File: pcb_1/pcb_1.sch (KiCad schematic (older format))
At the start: 32 parts, among them J1 Vin, J2 Vout, J3 2N3055_conn, P1 CONN_01X07, Q2 BD139, U1 MAX9944ASA+T, U2 MCP3422A0-E/SN, U3 MCP4822-E/SN, U4 INA213AIDCKT, U5 LM7705MM/NOPB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

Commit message: Mittauspinnit lisätty
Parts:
- added Cb6, Cb7: 0.1u, symbol C
- added P2, P3, P4, P5, P6, P7: CONN_01X01, symbol CONN_01X01
- added R6, R7: 10k, symbol R
- added U9: INA240A1PWR, symbol INA240A1PWR
- Rs1: value 0.05 -> 0.1
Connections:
- net +5V: now also U9.5 (OUT), U9.6 (VS)
- net -0.232V: now also P4.1 (P1)
- net GND: now also Cb6.2, Cb7.2, R7.2, U9.4 (NC), U9.7 (REF1)
- net at R3.2, R4.1, U1.2 (INA-)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: now also Cb6.1
- net at Cb2.1, U1.5 (INB+), U2.7 (CH2+): now also R6.2, R7.1; no longer U4.6 (OUT)
- net at Cb4.1, U1.6 (INB-), U3.6 (VoutB): now also P2.1 (P1)
- net at Cb3.1, U1.3 (INA+), U3.8 (VoutA): now also P3.1 (P1)
- net at J3.1, Rs1.1, U4.4 (IN+): now also U9.2 (GND)
- net at J2.2, R3.1, Rs1.2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: now also U9.3 (REF2)
- net at D1.2 (A), R1.1, R2.2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: now also P7.1 (P1)
- new net: R6.1, U4.6 (OUT), U9.8 (IN+)
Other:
- moved on the sheet: J2, R3, R4, U4

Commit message: AC-input lisätty Footprintit mikropiireille
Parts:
- Cb6, Cb7: footprint (none) -> Capacitors_SMD:C_0805_HandSoldering
- P2, P3, P4, P5, P6, P7: footprint (none) -> Pin_Headers:Pin_Header_Straight_1x01_Pitch2.54mm
- R6, R7: footprint (none) -> Resistors_SMD:R_0603_HandSoldering

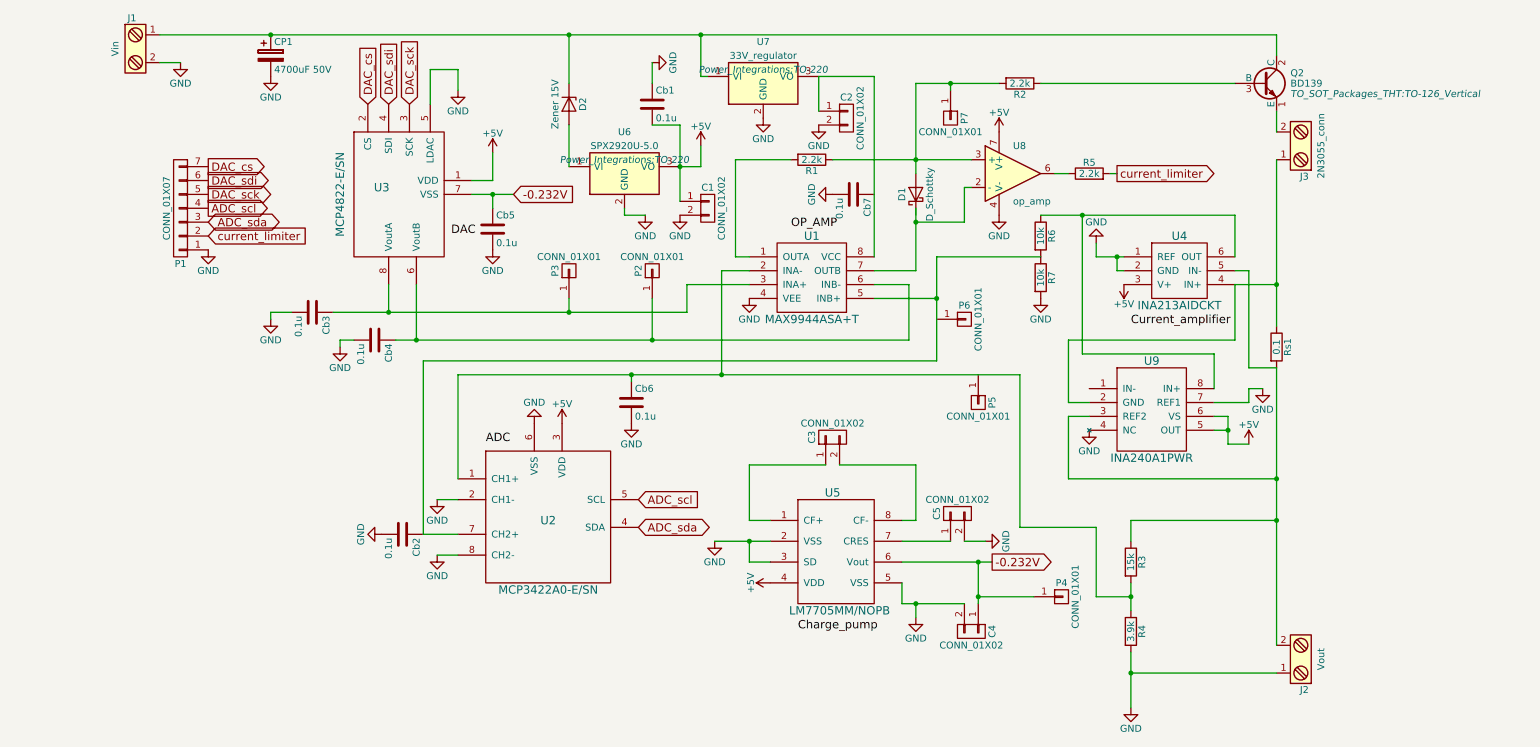
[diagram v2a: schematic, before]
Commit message: -Tasasuuntaajalle footprint footprints kansiossa -Oparille lisätty kapasitpanssipaikkoja
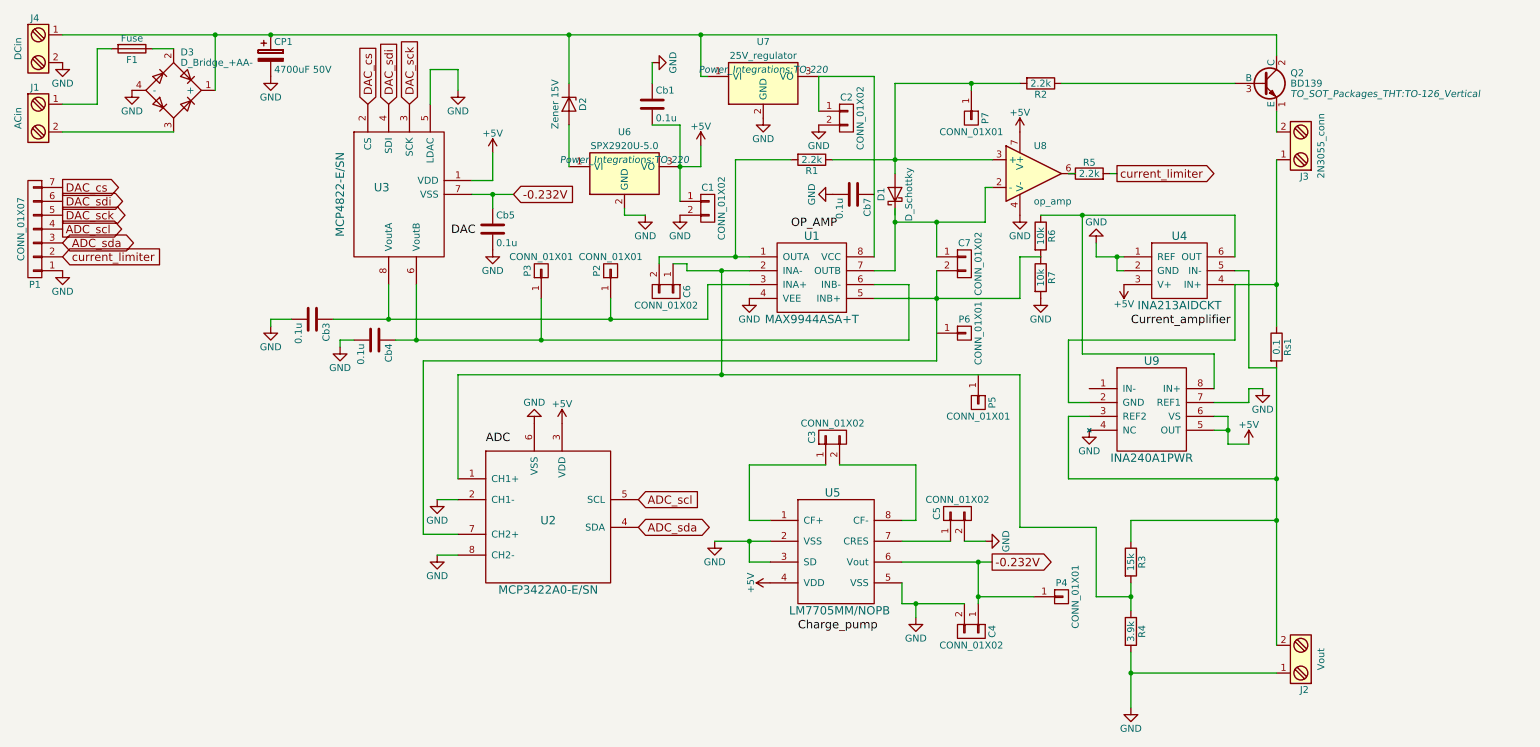
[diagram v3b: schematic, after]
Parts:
- removed Cb2, Cb6: 0.1u, Capacitors_SMD:C_0805_HandSoldering, symbol C
- added C6, C7: CONN_01X02, Pin_Headers:Pin_Header_Straight_1x02_Pitch2.54mm, symbol CONN_01X02
- added D3: D_Bridge_+AA-, lab_power_supply:GBU6D_diode-bridge, symbol D_Bridge_+AA-
- added F1: Fuse, symbol Fuse
- added J4: DCin, symbol Screw_Terminal_1x02
- J1: value Vin -> ACin
- U1, U2, U3, U5: footprint (none) -> Housings_SSOP:MSOP-8_3x3mm_Pitch0.65mm
- U4: footprint (none) -> TO_SOT_Packages_SMD:SOT-363_SC-70-6_Handsoldering
- U7: value 33V_regulator -> 25V_regulator
- U9: footprint (none) -> Housings_SSOP:TSSOP-8_4.4x3mm_Pitch0.65mm
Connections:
- net GND: now also D3.4 (-), J4.2; no longer J1.2
- net at R3.2, R4.1, U1.2 (INA-)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: now also C6.1 (P1)
- net at R6.2, R7.1, U1.5 (INB+)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: now also C7.2 (P2)
- net at Cb4.1, U1.6 (INB-), U3.6 (VoutB): now also P3.1 (P1); no longer P2.1 (P1)
- net at Cb3.1, U1.3 (INA+), U3.8 (VoutA): now also P2.1 (P1); no longer P3.1 (P1)
- net at R1.2, U1.1 (OUTA): now also C6.2 (P2)
- net at U1.7 (OUTB), U8.2 (-): now also C7.1 (P1)
- net at CP1.1, D2.1 (K), Q2.2 (C)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: now also D3.1 (+), J4.1; no longer J1.1
- new net: F1.2, J1.1
- new net: D3.3, J1.2
- new net: D3.2, F1.1
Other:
- moved on the sheet: Cb3, D1, J1, P1, P2, P3, P6, P7, R2, U8

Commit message: pcb suunniteltu
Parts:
- F1: footprint (none) -> Fuse_Holders_and_Fuses:Fuseholder5x20_horiz_SemiClosed_Casing10x25mm
- J1, J2, J3, J4: footprint (none) -> Wire_Connections_Bridges:WireConnection_2.50mmDrill_LargePad
- U8: footprint (none) -> Housings_SSOP:TSSOP-8_3x3mm_Pitch0.65mm
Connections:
- net ADC_scl: now also P1.3 (P3); no longer P1.4 (P4)
- net ADC_sda: now also P1.4 (P4); no longer P1.3 (P3)
- net DAC_sck: now also P1.6 (P6); no longer P1.5 (P5)
- net DAC_sdi: now also P1.5 (P5); no longer P1.6 (P6)
- net at C6.1 (P1), R3.2, R4.1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: now also P5.1 (P1)
- net at C7.2 (P2), R6.2, R7.1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: now also P6.1 (P1)
- net at C7.1 (P1), U1.7 (OUTB), U8.2 (-): now also D1.1 (K)
- net at C2.1 (P1), U1.8 (VCC), U7.3 (VO): now also Cb7.1
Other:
- moved on the sheet: Cb7, P5, P6
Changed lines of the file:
@@
 LIBS:contrib
 LIBS:valves
-LIBS:lab_power_supply
 LIBS:pcb_1-cache
 EELAYER 25 0
@@
 F 0 "J2" H 10650 5650 50  0000 C TNN
 F 1 "Vout" V 10500 5400 50  0000 C TNN
-F 2 "" H 10650 5175 50  0001 C CNN
+F 2 "Wire_Connections_Bridges:WireConnection_2.50mmDrill_LargePad" H 10650 5175 50  0001 C CNN
 F 3 "" H 10625 5400 50  0001 C CNN
 	1    10650 5400
@@
 Text GLabel 1700 2000 2    59   Output ~ 0
 DAC_cs
+Text GLabel 1700 2200 2    59   Output ~ 0
+DAC_sdi
 Text GLabel 1700 2100 2    59   Output ~ 0
-DAC_sdi
-Text GLabel 1700 2200 2    59   Output ~ 0
 DAC_sck
-Text GLabel 1700 2300 2    59   Output ~ 0
+Text GLabel 1700 2400 2    59   Output ~ 0
 ADC_scl
-Text GLabel 1700 2400 2    59   BiDi ~ 0
+Text GLabel 1700 2300 2    59   BiDi ~ 0
 ADC_sda
 $Comp
@@
 F 0 "U8" H 8700 2100 50  0000 L CNN
 F 1 "op_amp" H 8700 1700 50  0000 L CNN
-F 2 "" H 8750 2100 50  0001 C CNN
+F 2 "Housings_SSOP:TSSOP-8_3x3mm_Pitch0.65mm" H 8750 2100 50  0001 C CNN
 F 3 "" H 8700 2150 50  0000 C CNN
 	1    8700 1900
@@
 F 0 "J1" H 1500 1750 50  0000 C TNN
 F 1 "ACin" V 1350 1500 50  0000 C TNN
-F 2 "" H 1500 1275 50  0001 C CNN
+F 2 "Wire_Connections_Bridges:WireConnection_2.50mmDrill_LargePad" H 1500 1275 50  0001 C CNN
 F 3 "" H 1475 1500 50  0001 C CNN
 	1    1500 1500
@@
 F 0 "J3" H 10650 1950 50  0000 C TNN
 F 1 "2N3055_conn" V 10500 1700 50  0000 C TNN
-F 2 "" H 10650 1475 50  0001 C CNN
+F 2 "Wire_Connections_Bridges:WireConnection_2.50mmDrill_LargePad" H 10650 1475 50  0001 C CNN
 F 3 "" H 10625 1700 50  0001 C CNN
 	1    10650 1700
@@
 L C Cb7
 U 1 1 5DAB0730
-P 7400 2050
-F 0 "Cb7" H 7425 2150 50  0000 L CNN
-F 1 "0.1u" H 7425 1950 50  0000 L CNN
-F 2 "Capacitors_SMD:C_0805_HandSoldering" H 7438 1900 50  0001 C CNN
-F 3 "" H 7400 2050 50  0000 C CNN
-	1    7400 2050
+P 7350 2050
+F 0 "Cb7" H 7375 2150 50  0000 L CNN
+F 1 "0.1u" H 7375 1950 50  0000 L CNN
+F 2 "Capacitors_SMD:C_0805_HandSoldering" H 7388 1900 50  0001 C CNN
+F 3 "" H 7350 2050 50  0000 C CNN
+	1    7350 2050
 	0    1    1    0
 $EndComp
@@
 L GND #PWR028
 U 1 1 5DAB07B7
-P 7250 2050
-F 0 "#PWR028" H 7250 1800 50  0001 C CNN
-F 1 "GND" H 7250 1900 50  0000 C CNN
-F 2 "" H 7250 2050 50  0000 C CNN
-F 3 "" H 7250 2050 50  0000 C CNN
-	1    7250 2050
+P 7200 2050
+F 0 "#PWR028" H 7200 1800 50  0001 C CNN
+F 1 "GND" H 7200 1900 50  0000 C CNN
+F 2 "" H 7200 2050 50  0000 C CNN
+F 3 "" H 7200 2050 50  0000 C CNN
+	1    7200 2050
 	0    1    1    0
 $EndComp
@@
 L CONN_01X01 P6
 U 1 1 5DAB3A4E
-P 8200 3050
-F 0 "P6" H 8200 3150 50  0000 C CNN
-F 1 "CONN_01X01" V 8300 3050 50  0000 C CNN
-F 2 "Pin_Headers:Pin_Header_Straight_1x01_Pitch2.54mm" H 8200 3050 50  0001 C CNN
-F 3 "" H 8200 3050 50  0000 C CNN
-	1    8200 3050
+P 8250 3050
+F 0 "P6" H 8250 3150 50  0000 C CNN
+F 1 "CONN_01X01" V 8350 3050 50  0000 C CNN
+F 2 "Pin_Headers:Pin_Header_Straight_1x01_Pitch2.54mm" H 8250 3050 50  0001 C CNN
+F 3 "" H 8250 3050 50  0000 C CNN
+	1    8250 3050
 	1    0    0    -1
 $EndComp
@@
 L CONN_01X01 P5
 U 1 1 5DAB3E4B
-P 8300 3550
-F 0 "P5" H 8300 3650 50  0000 C CNN
-F 1 "CONN_01X01" V 8400 3550 50  0000 C CNN
-F 2 "Pin_Headers:Pin_Header_Straight_1x01_Pitch2.54mm" H 8300 3550 50  0001 C CNN
-F 3 "" H 8300 3550 50  0000 C CNN
-	1    8300 3550
+P 8300 3600
+F 0 "P5" H 8300 3700 50  0000 C CNN
+F 1 "CONN_01X01" V 8400 3600 50  0000 C CNN
+F 2 "Pin_Headers:Pin_Header_Straight_1x01_Pitch2.54mm" H 8300 3600 50  0001 C CNN
+F 3 "" H 8300 3600 50  0000 C CNN
+	1    8300 3600
 	0    1    1    0
 $EndComp
@@
 F 0 "J4" H 1500 1250 50  0000 C TNN
 F 1 "DCin" V 1350 1000 50  0000 C TNN
-F 2 "" H 1500 775 50  0001 C CNN
+F 2 "Wire_Connections_Bridges:WireConnection_2.50mmDrill_LargePad" H 1500 775 50  0001 C CNN
 F 3 "" H 1475 1000 50  0001 C CNN
 	1    1500 1000
@@
 F 0 "F1" V 2280 1000 50  0000 C CNN
 F 1 "Fuse" V 2125 1000 50  0000 C CNN
-F 2 "" V 2130 1000 50  0001 C CNN
+F 2 "Fuse_Holders_and_Fuses:Fuseholder5x20_horiz_SemiClosed_Casing10x25mm" V 2130 1000 50  0001 C CNN
 F 3 "" H 2200 1000 50  0000 C CNN
 	1    2200 1000
@@
 Connection ~ 7700 1800
 Wire Wire Line
-	7700 2150 7700 2600
-Wire Wire Line
 	7800 3100 7800 2700
 Wire Wire Line
@@
 Wire Wire Line
 	6000 2500 6000 2550
+Wire Wire Line
+	8300 3400 8300 3350
+Connection ~ 8300 3350
+Wire Wire Line
+	8050 3050 8000 3050
+Connection ~ 8000 3050
+Wire Wire Line
+	7500 2050 7550 2050
+Connection ~ 7550 2050
+Wire Wire Line
+	7700 2200 7700 2600
 $EndSCHEMATC

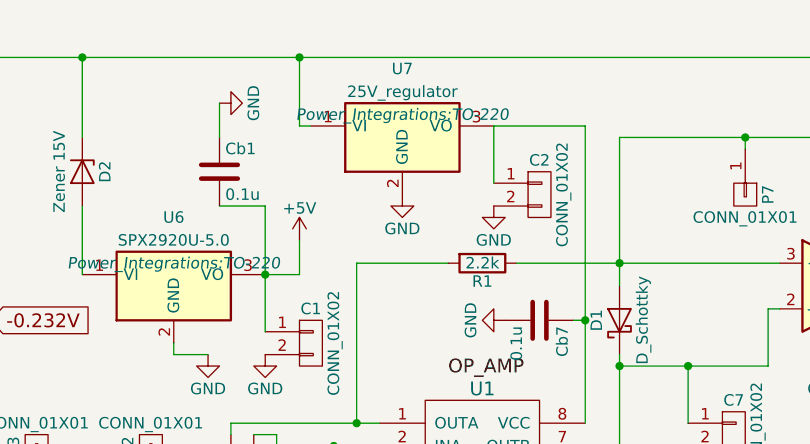
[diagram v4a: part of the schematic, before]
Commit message: Oparin regu vaihdettu ja konkkien footprintejä muutettu
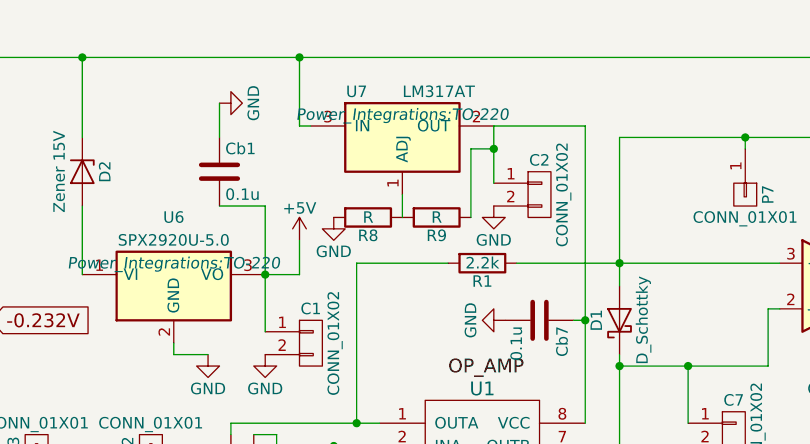
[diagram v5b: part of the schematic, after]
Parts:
- removed U7: 25V_regulator, Power_Integrations:TO-220, symbol SPX2920U-5.0
- added R8, R9: R, Resistors_SMD:R_0603_HandSoldering, symbol R
- added U7: LM317AT, Power_Integrations:TO-220, symbol LM317AT
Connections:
- net GND: now also R8.2
- net at C2.1 (P1), Cb7.1, U1.8 (VCC): now also R9.1, U7.2 (OUT)
- net at CP1.1, D2.1 (K), D3.1 (+)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: now also U7.3 (IN)
- new net: R8.1, R9.2, U7.1 (ADJ)
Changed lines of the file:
@@
 LIBS:contrib
 LIBS:valves
+LIBS:lab_power_supply
 LIBS:pcb_1-cache
 EELAYER 25 0
@@
 $EndComp
 $Comp
-L SPX2920U-5.0 U7
-U 1 1 5DA9E748
-P 6750 1250
-F 0 "U7" H 6750 1550 50  0000 C CNN
-F 1 "25V_regulator" H 6750 1450 50  0000 C CNN
-F 2 "Power_Integrations:TO-220" H 6750 1350 50  0000 C CIN
-F 3 "" H 6750 1250 50  0000 C CNN
-	1    6750 1250
-	1    0    0    -1
-$EndComp
-$Comp
 L GND #PWR015
 U 1 1 5DA9E862
-P 6750 1500
-F 0 "#PWR015" H 6750 1250 50  0001 C CNN
-F 1 "GND" H 6750 1350 50  0000 C CNN
-F 2 "" H 6750 1500 50  0000 C CNN
-F 3 "" H 6750 1500 50  0000 C CNN
-	1    6750 1500
+P 6450 1600
+F 0 "#PWR015" H 6450 1350 50  0001 C CNN
+F 1 "GND" H 6450 1450 50  0000 C CNN
+F 2 "" H 6450 1600 50  0000 C CNN
+F 3 "" H 6450 1600 50  0000 C CNN
+	1    6450 1600
 	1    0    0    -1
 $EndComp
@@
 Wire Wire Line
 	7700 2200 7700 2600
+$Comp
+L LM317AT U7
+U 1 1 5DAF6503
+P 6750 1250
+F 0 "U7" H 6550 1450 50  0000 C CNN
+F 1 "LM317AT" H 6750 1450 50  0000 L CNN
+F 2 "Power_Integrations:TO-220" H 6750 1350 50  0000 C CIN
+F 3 "" H 6750 1250 50  0000 C CNN
+	1    6750 1250
+	1    0    0    -1
+$EndComp
+$Comp
+L R R8
+U 1 1 5DAF6612
+P 6600 1600
+F 0 "R8" V 6680 1600 50  0000 C CNN
+F 1 "R" V 6600 1600 50  0000 C CNN
+F 2 "Resistors_SMD:R_0603_HandSoldering" V 6530 1600 50  0001 C CNN
+F 3 "" H 6600 1600 50  0000 C CNN
+	1    6600 1600
+	0    1    1    0
+$EndComp
+$Comp
+L R R9
+U 1 1 5DAF6707
+P 6900 1600
+F 0 "R9" V 6980 1600 50  0000 C CNN
+F 1 "R" V 6900 1600 50  0000 C CNN
+F 2 "Resistors_SMD:R_0603_HandSoldering" V 6830 1600 50  0001 C CNN
+F 3 "" H 6900 1600 50  0000 C CNN
+	1    6900 1600
+	0    1    1    0
+$EndComp
+Wire Wire Line
+	7050 1600 7050 1300
+Wire Wire Line
+	7050 1300 7150 1300
+Connection ~ 7150 1300
+Wire Wire Line
+	6750 1600 6750 1500
 $EndSCHEMATC

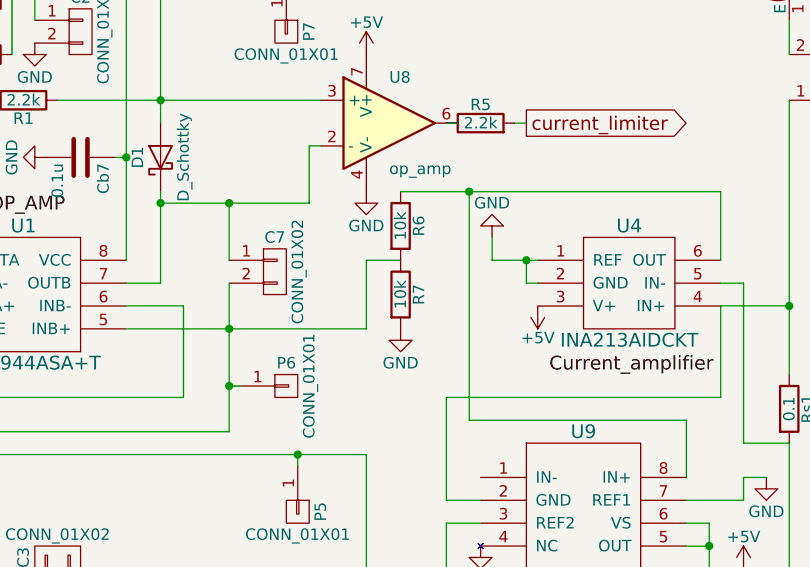
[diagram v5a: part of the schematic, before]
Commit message: Traceja paksunnettu
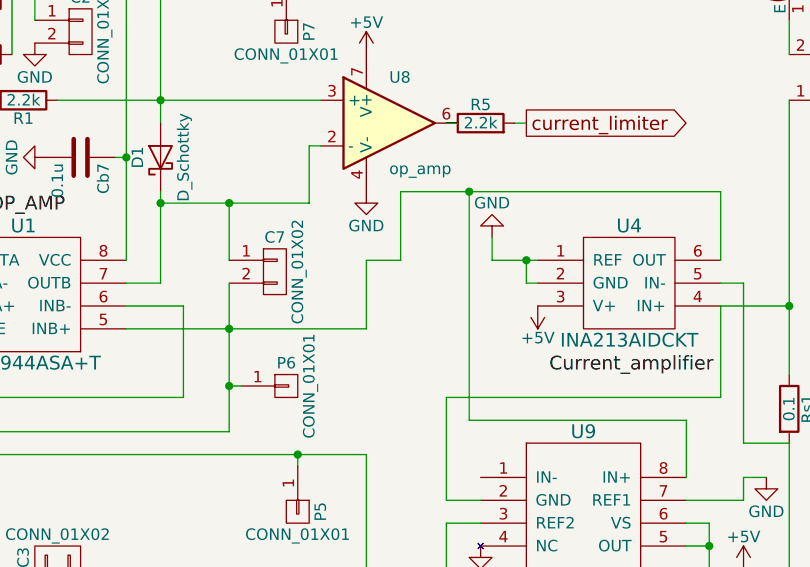
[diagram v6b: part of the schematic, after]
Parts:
- removed R6, R7: 10k, Resistors_SMD:R_0603_HandSoldering, symbol R
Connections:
- net at C7.2 (P2), P6.1 (P1), U1.5 (INB+)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: now also U4.6 (OUT), U9.8 (IN+)
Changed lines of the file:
@@
-$EndComp
-$Comp
-L R R6
-U 1 1 5DAB43DD
-P 8750 2350
-F 0 "R6" V 8830 2350 50  0000 C CNN
-F 1 "10k" V 8750 2350 50  0000 C CNN
-F 2 "Resistors_SMD:R_0603_HandSoldering" V 8680 2350 50  0001 C CNN
-F 3 "" H 8750 2350 50  0000 C CNN
-	1    8750 2350
-	1    0    0    -1
-$EndComp
-$Comp
-L R R7
-U 1 1 5DAB44DA
-P 8750 2650
-F 0 "R7" V 8830 2650 50  0000 C CNN
-F 1 "10k" V 8750 2650 50  0000 C CNN
-F 2 "Resistors_SMD:R_0603_HandSoldering" V 8680 2650 50  0001 C CNN
-F 3 "" H 8750 2650 50  0000 C CNN
-	1    8750 2650
-	1    0    0    -1
-$EndComp
-$Comp
-L GND #PWR029
-U 1 1 5DAB472A
-P 8750 2800
-F 0 "#PWR029" H 8750 2550 50  0001 C CNN
-F 1 "GND" H 8750 2650 50  0000 C CNN
-F 2 "" H 8750 2800 50  0000 C CNN
-F 3 "" H 8750 2800 50  0000 C CNN
-	1    8750 2800
-	1    0    0    -1
 $EndComp
 $Comp
@@
 $EndComp
 $Comp
-L GND #PWR030
+L GND #PWR029
 U 1 1 5DAB6D92
 P 9100 3750
-F 0 "#PWR030" H 9100 3500 50  0001 C CNN
+F 0 "#PWR029" H 9100 3500 50  0001 C CNN
 F 1 "GND" H 9100 3600 50  0000 C CNN
 F 2 "" H 9100 3750 50  0000 C CNN
@@
 $EndComp
 $Comp
-L GND #PWR031
+L GND #PWR030
 U 1 1 5DAB710F
 P 10350 3450
-F 0 "#PWR031" H 10350 3200 50  0001 C CNN
+F 0 "#PWR030" H 10350 3200 50  0001 C CNN
 F 1 "GND" H 10350 3300 50  0000 C CNN
 F 2 "" H 10350 3450 50  0000 C CNN
@@
 $EndComp
 $Comp
-L +5V #PWR032
+L +5V #PWR031
 U 1 1 5DAB72B5
 P 10250 3850
-F 0 "#PWR032" H 10250 3700 50  0001 C CNN
+F 0 "#PWR031" H 10250 3700 50  0001 C CNN
 F 1 "+5V" H 10250 3990 50  0000 C CNN
 F 2 "" H 10250 3850 50  0000 C CNN
@@
 $EndComp
 $Comp
-L GND #PWR033
+L GND #PWR032
 U 1 1 5DABB706
 P 2200 1300
-F 0 "#PWR033" H 2200 1050 50  0001 C CNN
+F 0 "#PWR032" H 2200 1050 50  0001 C CNN
 F 1 "GND" H 2200 1150 50  0000 C CNN
 F 2 "" H 2200 1300 50  0000 C CNN
@@
 $EndComp
 $Comp
-L GND #PWR034
+L GND #PWR033
 U 1 1 5DABD497
 P 1700 1100
-F 0 "#PWR034" H 1700 850 50  0001 C CNN
+F 0 "#PWR033" H 1700 850 50  0001 C CNN
 F 1 "GND" H 1700 950 50  0000 C CNN
 F 2 "" H 1700 1100 50  0000 C CNN
@@
 Wire Wire Line
 	6750 1600 6750 1500
+Wire Wire Line
+	8750 2500 8750 2200
 $EndSCHEMATC
